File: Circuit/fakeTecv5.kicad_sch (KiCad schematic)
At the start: 72 parts, among them J1 EXTRA, J11 FET1 3,3, J12 FET2 3,3, J13 FET3 3,3, J14 GPS Pins, J16 Encoder Pads, J37 SCL, J38 JST-SH-4, J39 SDA, J40 3.3V, J41 GND, J42 FET1, J43 FET2, J44 FET3, J45 GND, J47 GND, J48 GND, J49 GND, J5 I2C Oled screen, J6 FET1 Drain, J7 FET2 Drain, J8 FET3 Drain, J9 Molex PicoBlade 0532610271, M1 ERM Motor, Q1 AO3400A, Q2 AO3400A, Q3 AO3400A, SW1 Reset, SW2 SW_Push, SW3 RotaryEncoder_Switch, U1 XB8089D0, U2 HT-RA62, U3 nice!nano v2

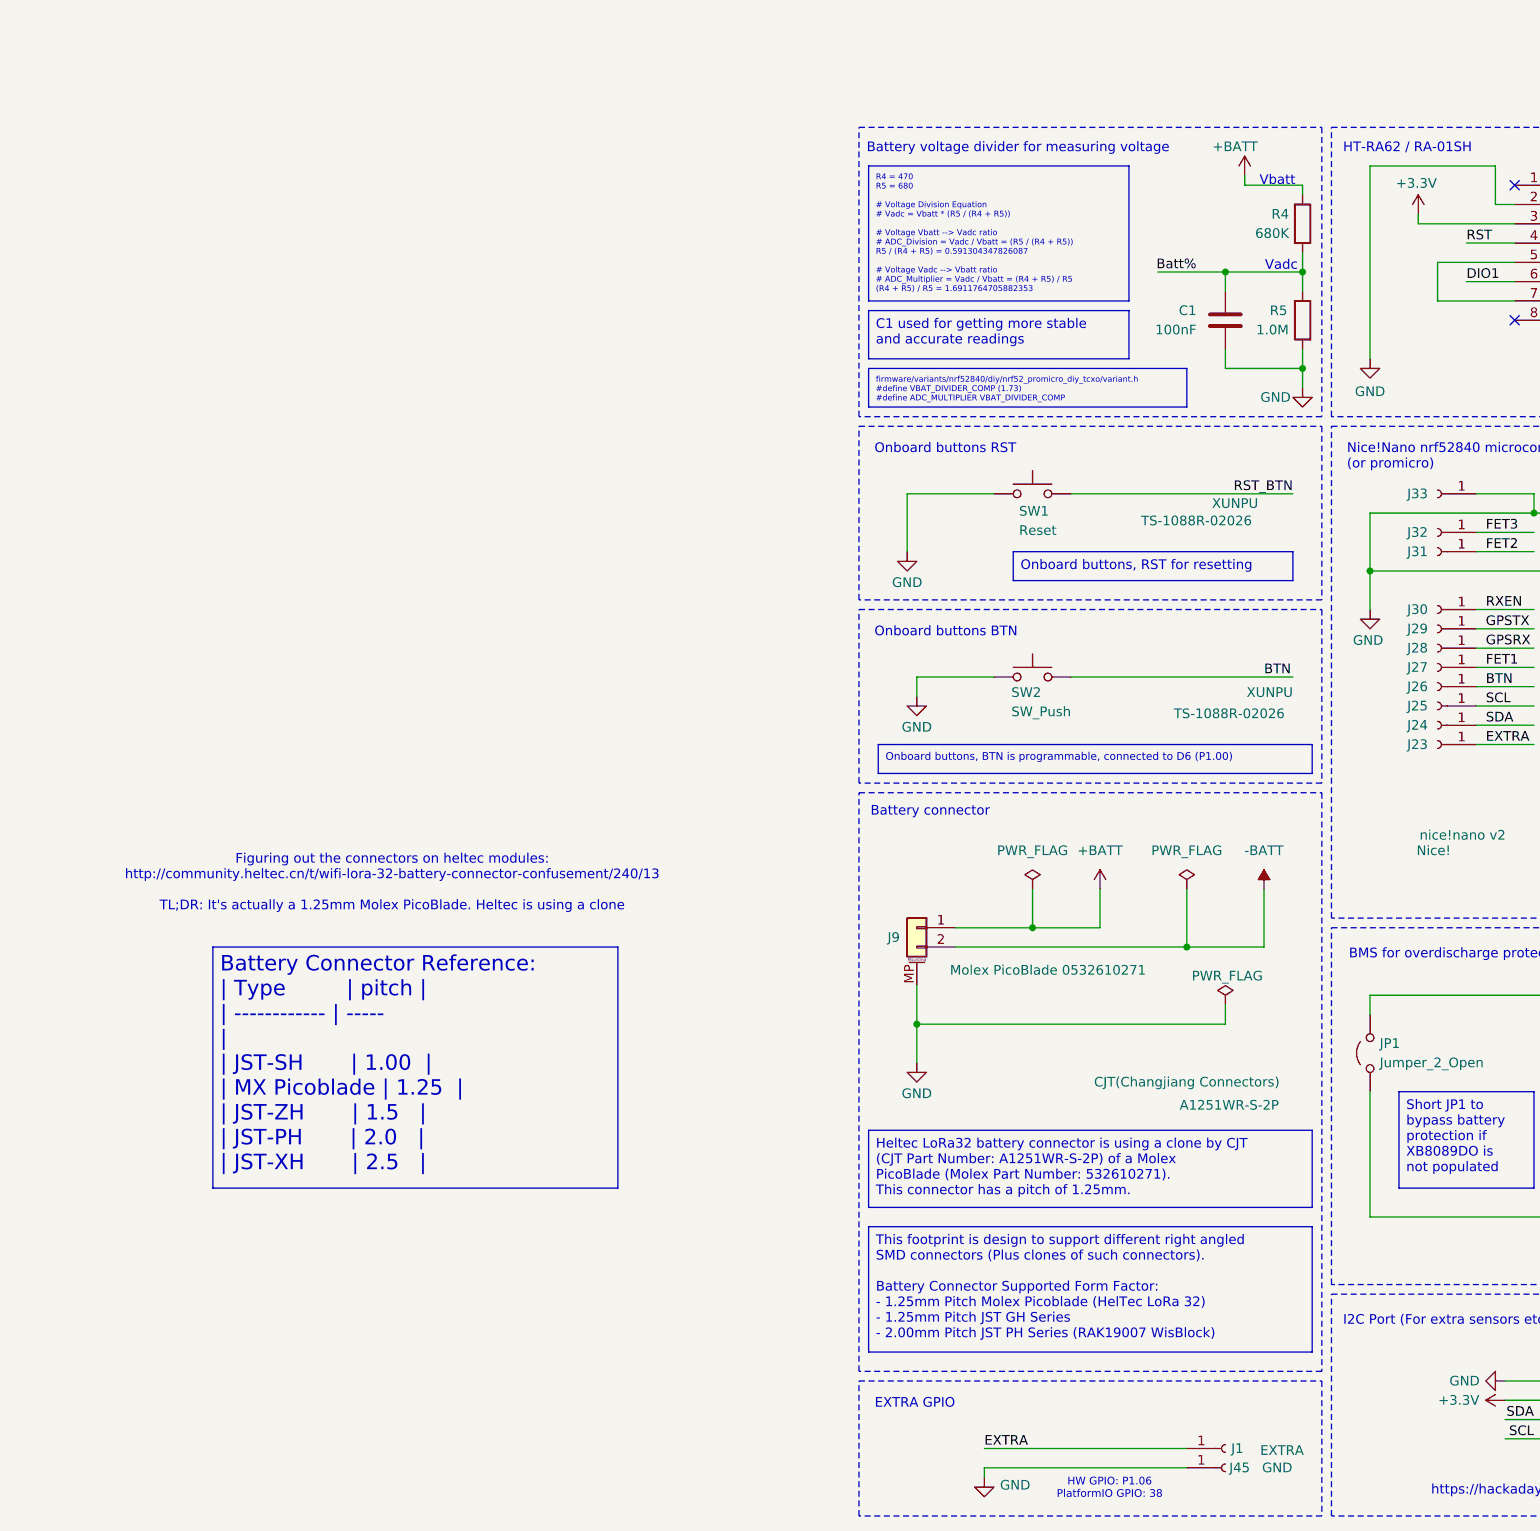
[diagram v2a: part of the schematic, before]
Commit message: hw: Update schematic and connector to clarify battery connector
Including some photos and directions on locating the correct parts
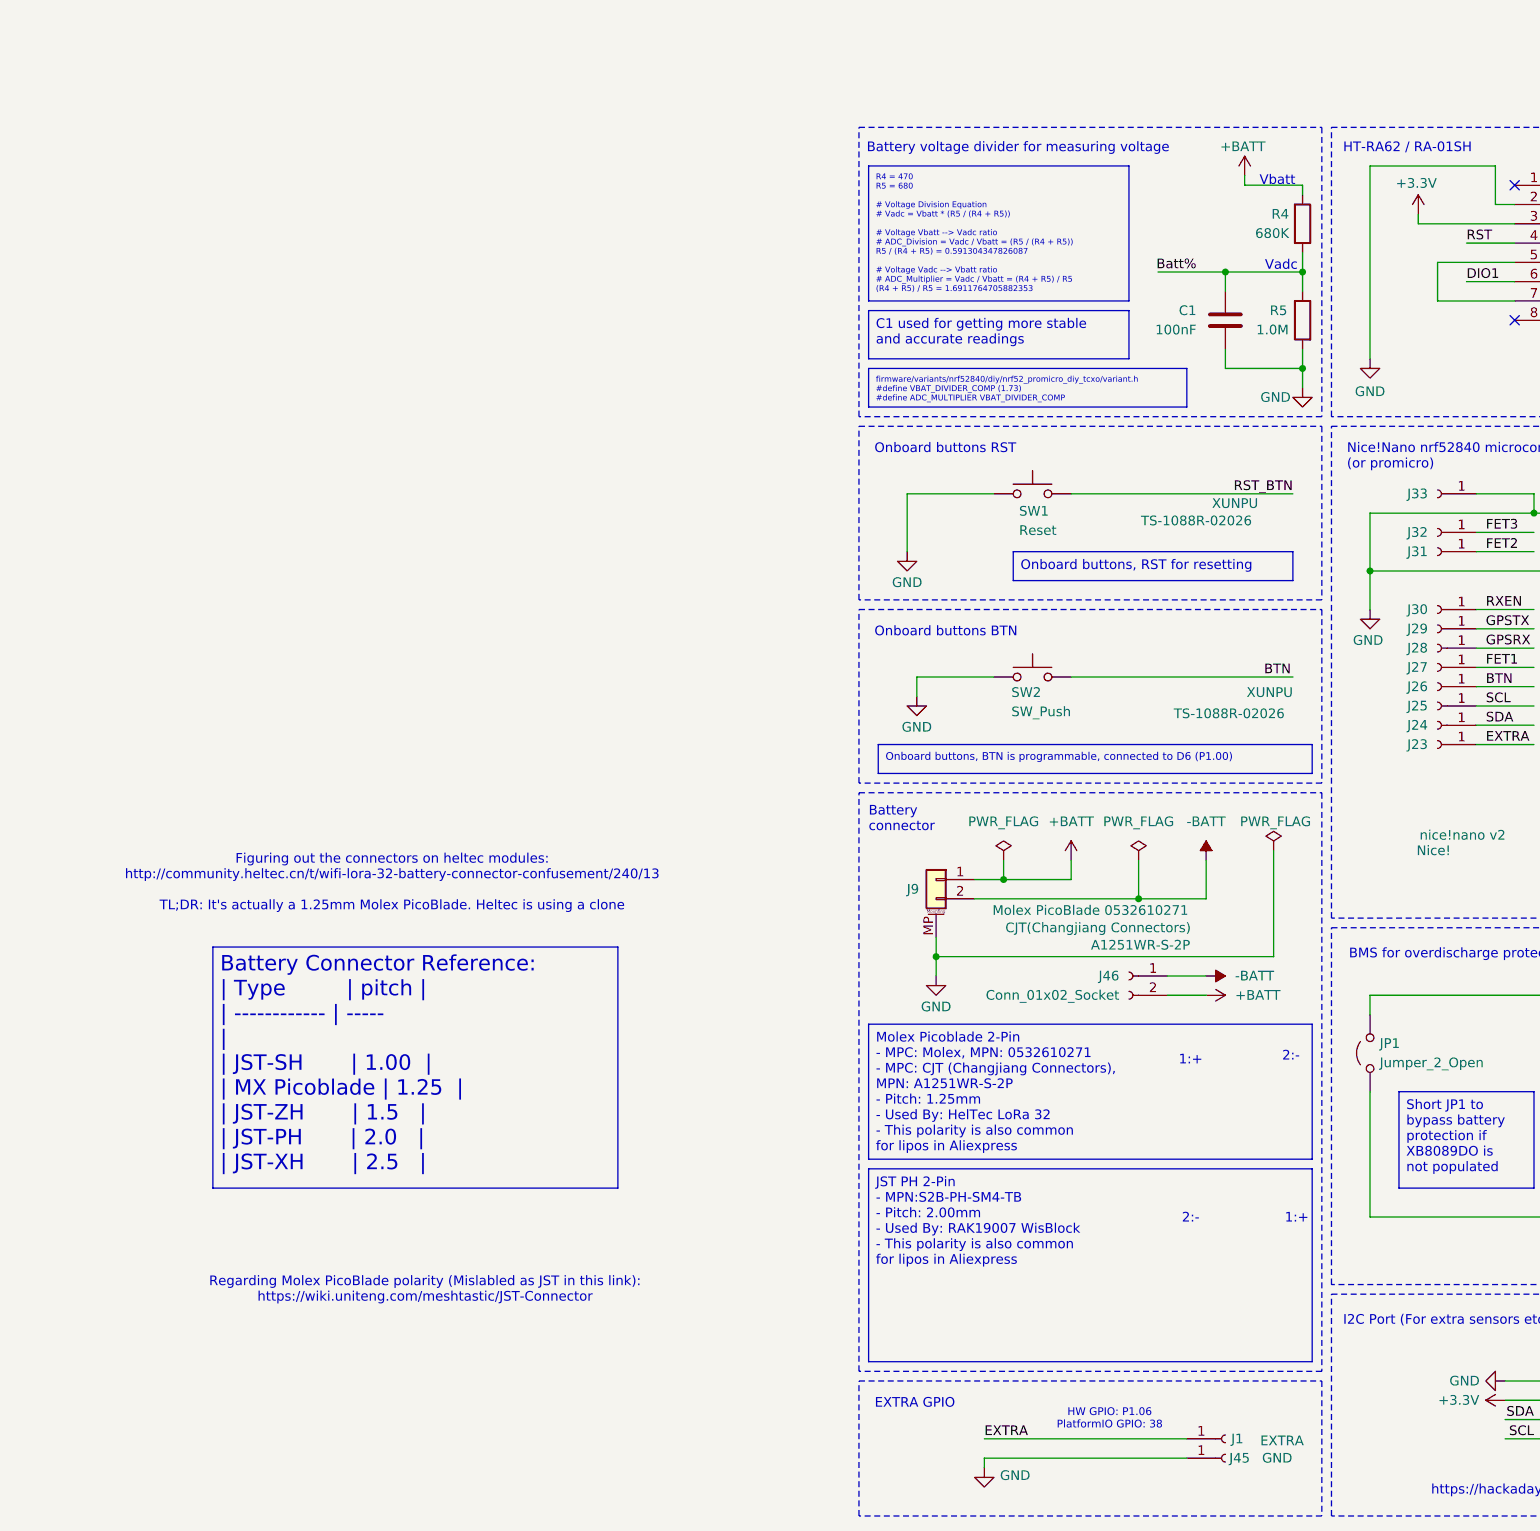
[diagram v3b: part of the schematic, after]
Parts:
- added J46: Conn_01x02_Socket, faketec:wirebond battery header, symbol Connector:Conn_01x02_Socket
- J16: now left out of the parts list
- J9: footprint faketec:JST_PH_S2B-PH-SM4-TB_1x02-1MP_P2.00mm_Horizontal -> faketec:Combined_Battery_Connector_Molex_PicoBlade_P1.00_And_JST_PH_2.00mm
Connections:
- net +BATT: now also J46.2 (Pin_2)
- net -BATT: now also J46.1 (Pin_1)
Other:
- note added: "1:+"
- note added: "2:-"
- note added: "Regarding Molex PicoBlade polarity (Mislabled as JST in this link): https://wiki.uniteng.com/meshtastic/JST-Connector"
- moved on the sheet: J1, J45, J9

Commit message: hw: Text Variable. Also mark as Rev5.
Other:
- title: roTec v5 (faketec v5 fork) -> roTec Rev${REVISION}
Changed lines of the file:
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@@
 	(paper "A4")
 	(title_block
-		(title "roTec v5 (faketec v5 fork)")
-		(date "2025-03-19")
-		(rev "4")
+		(title "roTec Rev${REVISION}")
+		(date "2025-12-25")
+		(rev "${REVISION}")
+		(comment 1 "Fork Of FakeTec (https://github.com/gargomoma/fakeTec_pcb/)")
+		(comment 2 "Development Source: https://github.com/mofosyne/roTec_pcb")
 	)
 	(rectangle

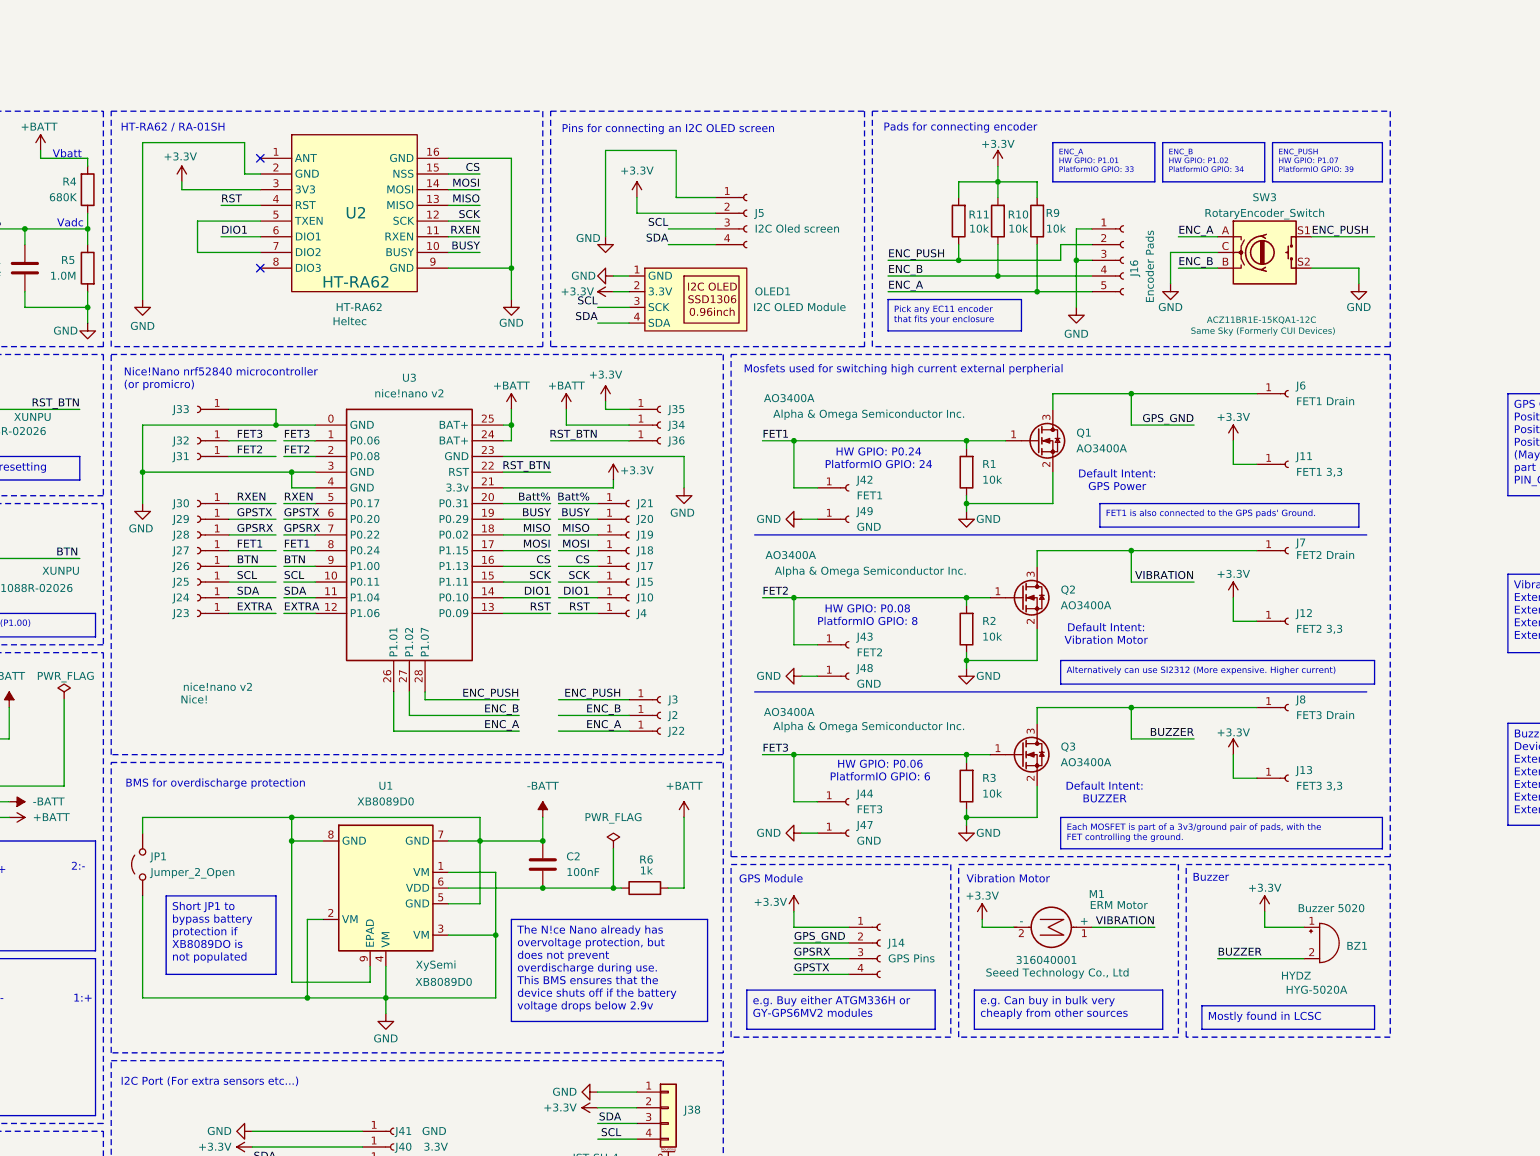
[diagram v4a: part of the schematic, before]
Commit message: hw: Add JST-SH-4 for encoder. Marked as Rev5.1
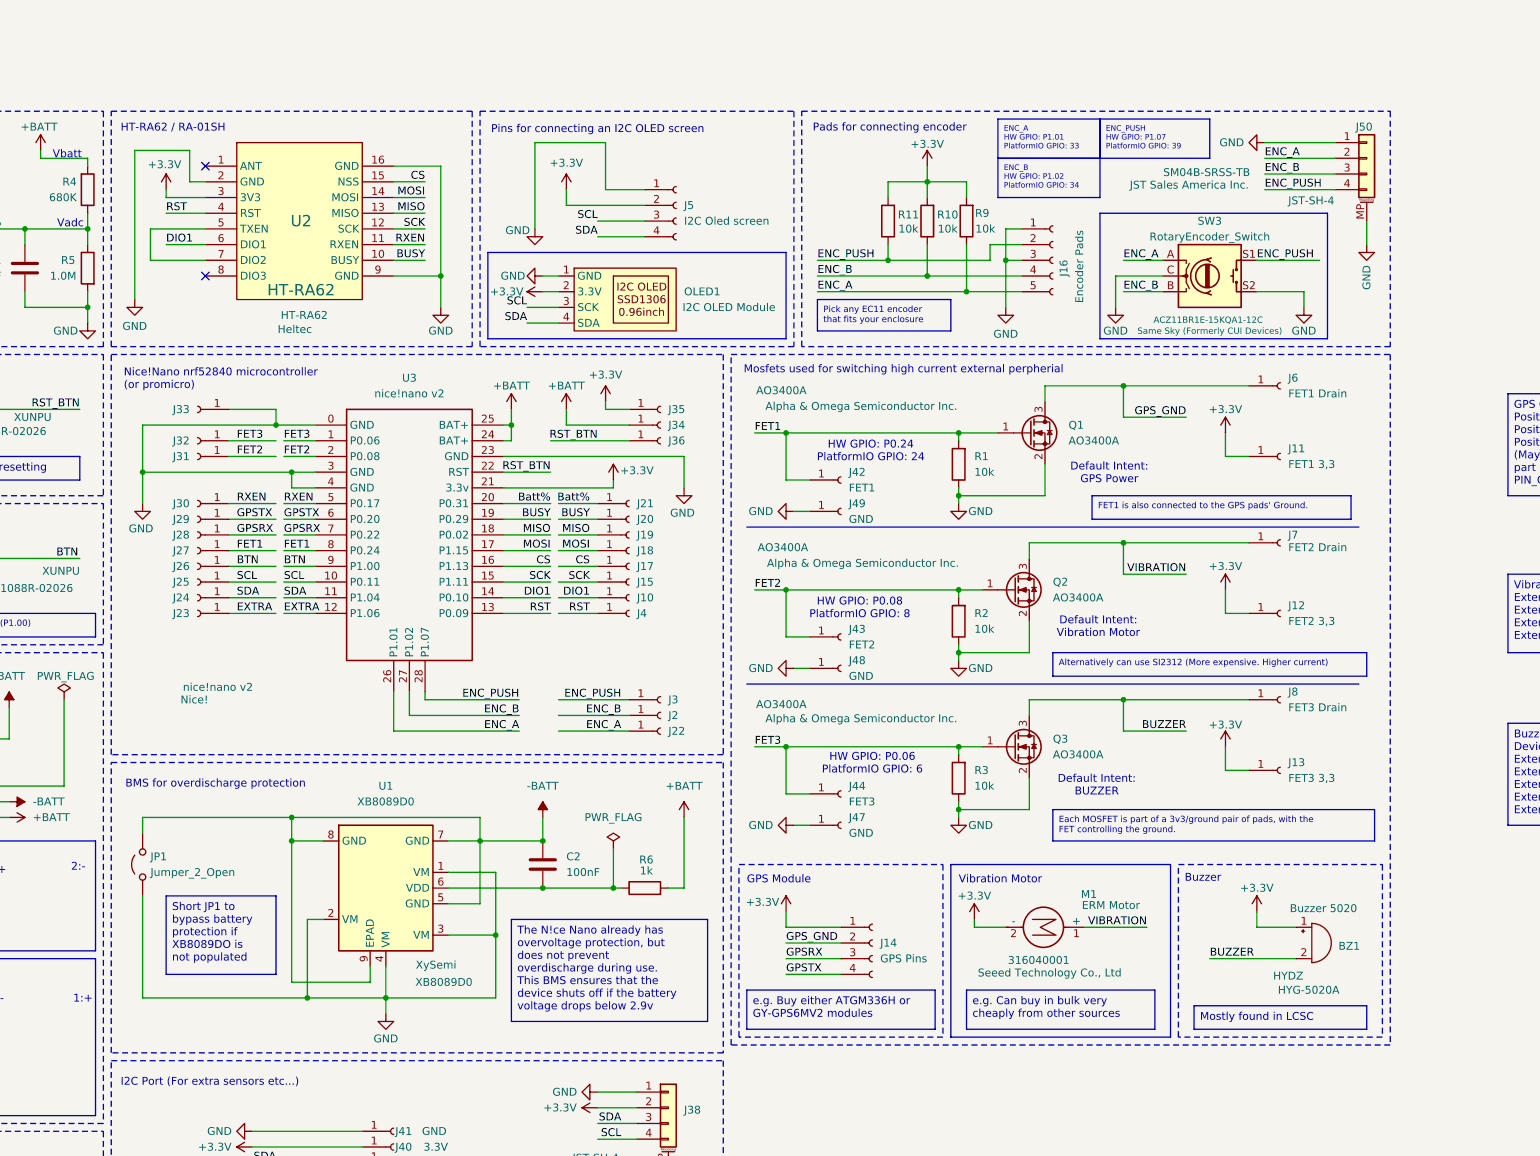
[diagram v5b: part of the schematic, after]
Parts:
- added J50: JST-SH-4, Connector_JST:JST_SH_SM04B-SRSS-TB_1x04-1MP_P1.00mm_Horizontal, symbol Connector_Generic_MountingPin:Conn_01x04_MountingPin
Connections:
- net ENC_A: now also J50.2 (Pin_2)
- net ENC_B: now also J50.3 (Pin_3)
- net ENC_PUSH: now also J50.4 (Pin_4)
- net GND: now also J50.1 (Pin_1), J50.MP (MountPin)
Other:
- moved on the sheet: BZ1, J11, J12, J13, J14, J16, J42, J43, J44, J47, J48, J49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
